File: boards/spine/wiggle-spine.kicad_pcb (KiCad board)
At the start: 2 copper layers, 114.3 x 88.9 mm, 187 parts, among them CON1 USB-B, CON2 XLR-3 Female, CON3 USB-A, CON4 2.5mm 5-24V 5A, CON5 5-24V 16A, CON6 PLR135, CON7 PLT133, Q1 DMN3190LDW, Q2 2N7002P, Q3 AOD4189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

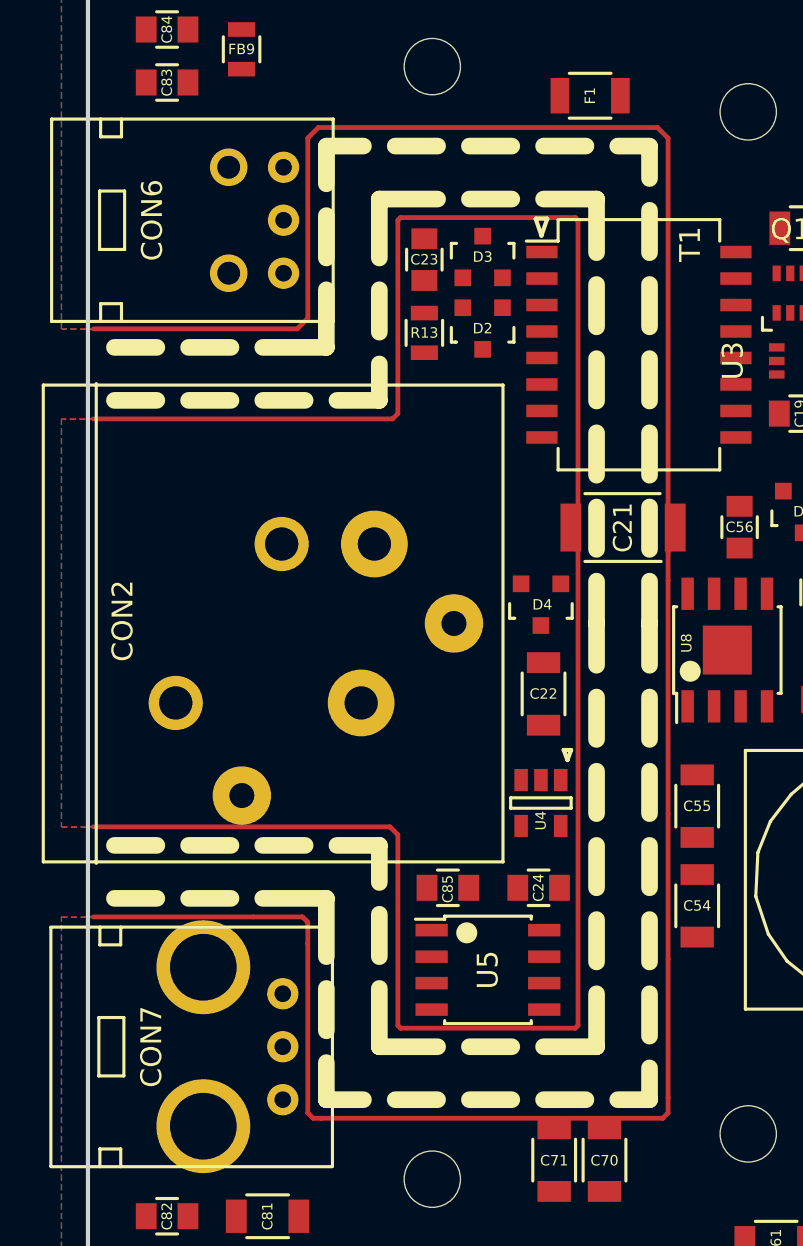
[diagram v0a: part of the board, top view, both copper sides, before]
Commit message: Hand edit to duplicate gap boundaries on bottom layer
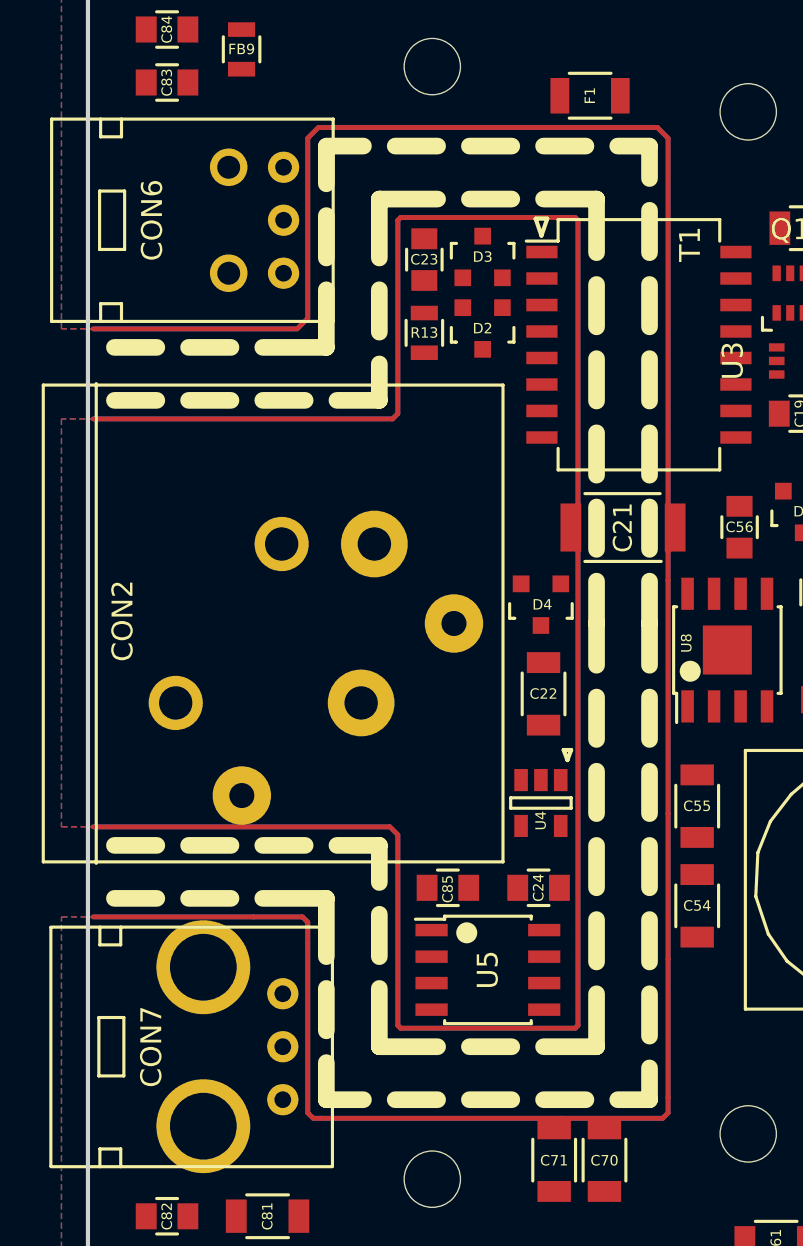
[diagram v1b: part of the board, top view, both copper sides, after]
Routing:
- net GND: track 120.9 -> 241.7 mm
- net /DMX512/DMXGND: track 104.3 -> 208.5 mm
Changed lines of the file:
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@@
   (segment (start 108.585 105.664) (end 108.585 82.129) (width 0.2286) (layer F.Cu) (net 172))
   (segment (start 108.585 82.129) (end 108.244 81.788) (width 0.2286) (layer F.Cu) (net 172))
+  (segment (start 112.649 110.109) (end 107.823 110.109) (width 0.2286) (layer B.Cu) (net 136))
+  (segment (start 93.035 100.457) (end 85.344 100.457) (width 0.2286) (layer B.Cu) (net 136))
+  (segment (start 95.377 100.457) (end 93.035 100.457) (width 0.2286) (layer B.Cu) (net 136))
+  (segment (start 95.540001 100.620001) (end 95.377 100.457) (width 0.2286) (layer B.Cu) (net 136))
+  (segment (start 95.631 100.711) (end 95.540001 100.620001) (width 0.2286) (layer B.Cu) (net 136))
+  (segment (start 95.631 101.727) (end 95.631 100.711) (width 0.2286) (layer B.Cu) (net 136))
+  (segment (start 95.631 109.855) (end 95.631 101.727) (width 0.2286) (layer B.Cu) (net 136))
+  (segment (start 95.885 110.109) (end 95.631 109.855) (width 0.2286) (layer B.Cu) (net 136))
+  (segment (start 96.266 110.109) (end 95.885 110.109) (width 0.2286) (layer B.Cu) (net 136))
+  (segment (start 107.823 110.109) (end 96.266 110.109) (width 0.2286) (layer B.Cu) (net 136))
+  (segment (start 112.903 109.855) (end 112.649 110.109) (width 0.2286) (layer B.Cu) (net 136))
+  (segment (start 112.903 109.118392) (end 112.903 109.855) (width 0.2286) (layer B.Cu) (net 136))
+  (segment (start 112.903 102.489) (end 112.903 109.118392) (width 0.2286) (layer B.Cu) (net 136))
+  (segment (start 112.903 95.504) (end 112.903 102.489) (width 0.2286) (layer B.Cu) (net 136))
+  (segment (start 112.903 84.328) (end 112.903 95.504) (width 0.2286) (layer B.Cu) (net 136))
+  (segment (start 112.903 84.328) (end 112.903 82.931) (width 0.2286) (layer B.Cu) (net 136))
+  (segment (start 113.244 82.59) (end 113.244 81.788) (width 0.2286) (layer B.Cu) (net 136))
+  (segment (start 112.903 82.931) (end 113.244 82.59) (width 0.2286) (layer B.Cu) (net 136))
+  (segment (start 85.344 72.263) (end 95.123 72.263) (width 0.2286) (layer B.Cu) (net 136))
+  (segment (start 112.395 62.611) (end 112.903 63.119) (width 0.2286) (layer B.Cu) (net 136))
+  (segment (start 112.903 81.447) (end 113.244 81.788) (width 0.2286) (layer B.Cu) (net 136))
+  (segment (start 95.123 72.263) (end 95.631 71.755) (width 0.2286) (layer B.Cu) (net 136))
+  (segment (start 95.631 71.755) (end 95.631 63.119) (width 0.2286) (layer B.Cu) (net 136))
+  (segment (start 95.631 63.119) (end 96.139 62.611) (width 0.2286) (layer B.Cu) (net 136))
+  (segment (start 96.139 62.611) (end 112.395 62.611) (width 0.2286) (layer B.Cu) (net 136))
+  (segment (start 112.903 63.119) (end 112.903 81.447) (width 0.2286) (layer B.Cu) (net 136))
+  (segment (start 85.344 76.581) (end 99.695 76.581) (width 0.2286) (layer B.Cu) (net 172))
+  (segment (start 99.949 67.056) (end 100.076 66.929) (width 0.2286) (layer B.Cu) (net 172))
+  (segment (start 108.585 81.447) (end 108.244 81.788) (width 0.2286) (layer B.Cu) (net 172))
+  (segment (start 99.695 76.581) (end 99.949 76.327) (width 0.2286) (layer B.Cu) (net 172))
+  (segment (start 99.949 76.327) (end 99.949 67.056) (width 0.2286) (layer B.Cu) (net 172))
+  (segment (start 100.076 66.929) (end 108.458 66.929) (width 0.2286) (layer B.Cu) (net 172))
+  (segment (start 108.458 66.929) (end 108.585 67.056) (width 0.2286) (layer B.Cu) (net 172))
+  (segment (start 108.585 67.056) (end 108.585 81.447) (width 0.2286) (layer B.Cu) (net 172))
+  (segment (start 85.344 96.139) (end 99.568 96.139) (width 0.2286) (layer B.Cu) (net 172))
+  (segment (start 99.568 96.139) (end 99.949 96.52) (width 0.2286) (layer B.Cu) (net 172))
+  (segment (start 99.949 96.52) (end 99.949 105.664) (width 0.2286) (layer B.Cu) (net 172))
+  (segment (start 99.949 105.664) (end 100.076 105.791) (width 0.2286) (layer B.Cu) (net 172))
+  (segment (start 100.076 105.791) (end 108.458 105.791) (width 0.2286) (layer B.Cu) (net 172))
+  (segment (start 108.458 105.791) (end 108.585 105.664) (width 0.2286) (layer B.Cu) (net 172))
+  (segment (start 108.585 105.664) (end 108.585 82.129) (width 0.2286) (layer B.Cu) (net 172))
+  (segment (start 108.585 82.129) (end 108.244 81.788) (width 0.2286) (layer B.Cu) (net 172))
   (zone (net 136) (net_name GND) (layer F.Cu) (hatch edge 0.508)
     (connect_pads yes (clearance 0.381))

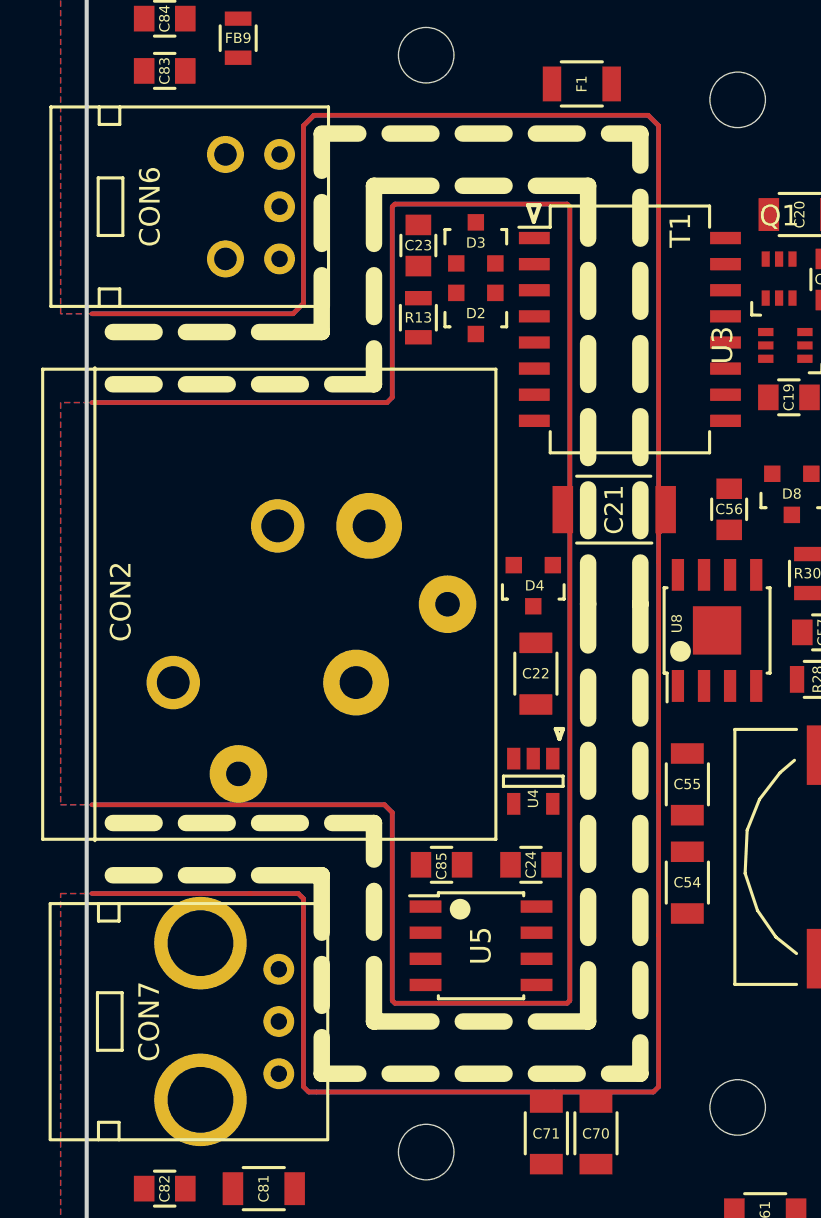
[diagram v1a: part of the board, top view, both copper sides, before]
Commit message: Via stitching and net fixes for DMXGND
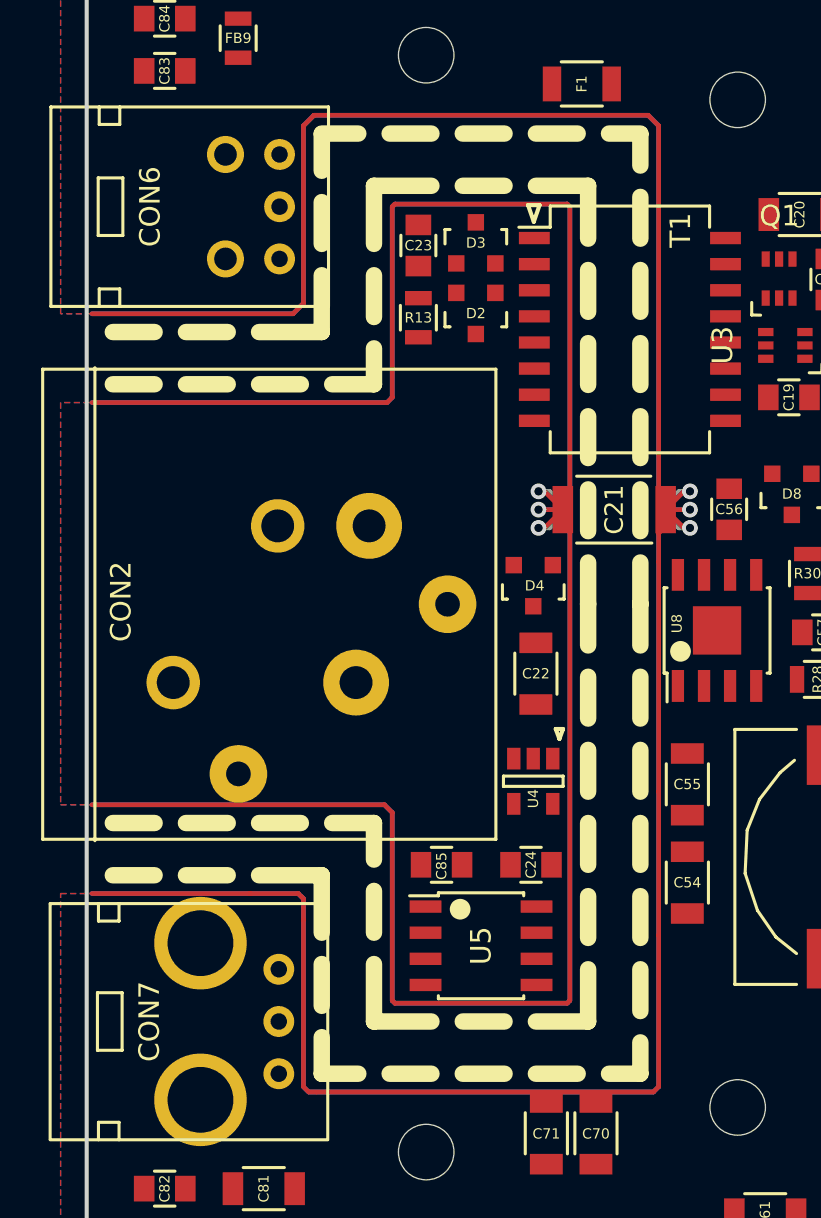
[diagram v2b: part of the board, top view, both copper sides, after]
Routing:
- net GND: track 241.7 -> 250.9 mm, vias 0 -> 3
- net /DMX512/DMXGND: track 208.5 -> 217.7 mm, vias 0 -> 3

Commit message: More zone placement.. concerned about +24
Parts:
- moved R20 46.5 mm to (156.0, 77.0), turned to 180 degrees
- moved C73 16.9 mm to (183.6, 69.6), turned to 0 degrees
- moved R35 11.8 mm to (181.3, 67.3), turned to 0 degrees
- moved D9 11.7 mm to (177.5, 67.8), turned to 0 degrees
- moved FB3 9.80 mm to (172.0, 81.8), turned to 0 degrees
- moved C72 2.92 mm to (188.7, 65.3)
- moved R17 2.79 mm to (197.4, 54.2)
- moved R19 2.79 mm to (193.3, 54.2)
- moved R18 2.79 mm to (195.3, 54.2)
- moved C1 1.42 mm to (165.9, 79.0)
- moved C43 0.64 mm to (170.7, 74.5)
- moved C44 0.51 mm to (178.1, 74.5)
- moved Q3 0.25 mm to (183.6, 56.4)
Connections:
- net Net-(C72-Pad2) renamed /Power/5-24V Power Input/POWER_IN
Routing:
- net +24V: track 0.00 -> 245.4 mm
- net GNDPWR: track 0.00 -> 62.8 mm
- net /Power/5-24V Power Input/POWER_IN: track 0.00 -> 25.8 mm
- net GND: track 250.9 -> 268.7 mm
- net +5V: track 0.00 -> 17.8 mm
- net +3V3: track 0.00 -> 17.8 mm
- net Net-(D9-Pad3): track 0.00 -> 13.3 mm
- added copper zone on F.Cu, net +24V
- added copper zone on F.Cu, net /Power/5-24V Power Input/POWER_IN
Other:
- net class ExtPower removed
- net class ProtectiveGround removed

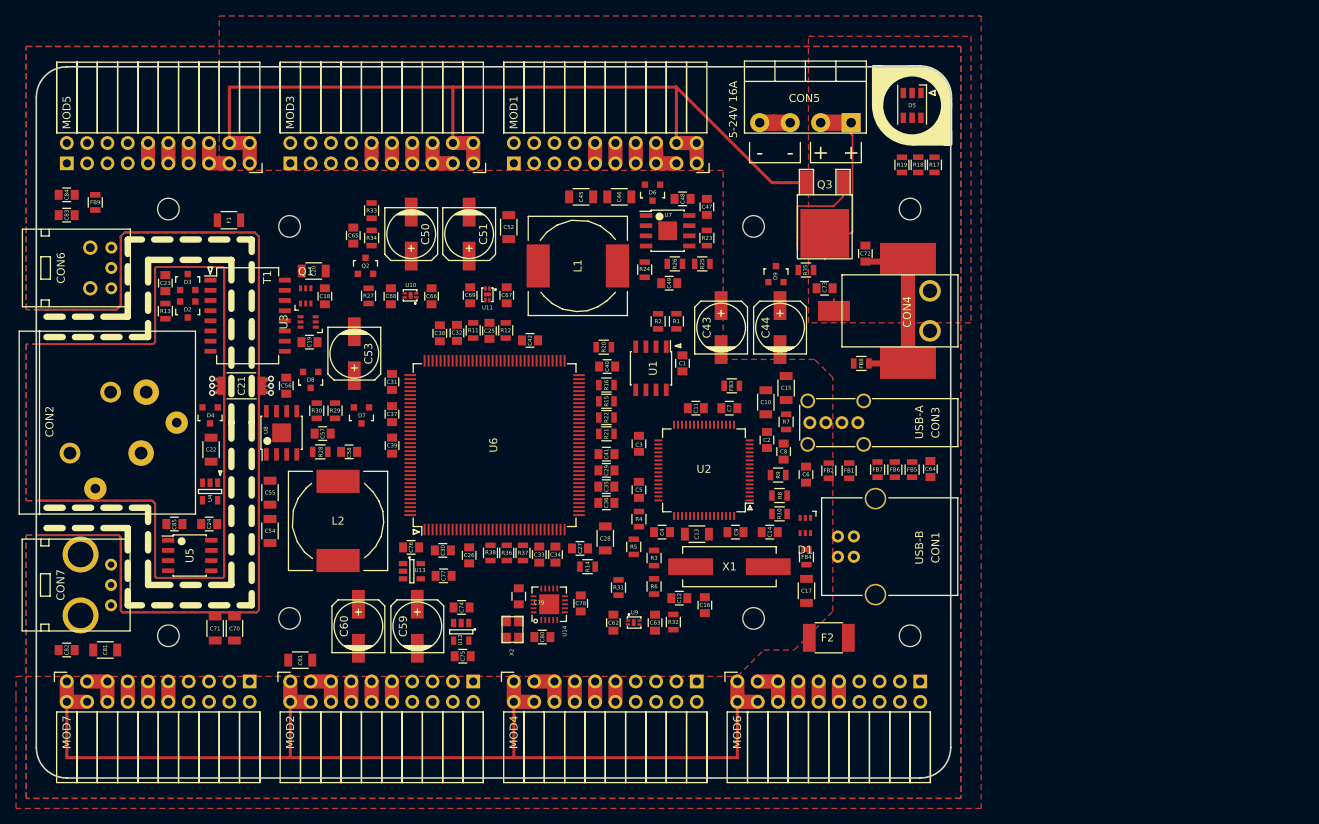
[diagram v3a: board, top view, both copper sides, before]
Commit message: Progress on zone and 3v3 filter layout
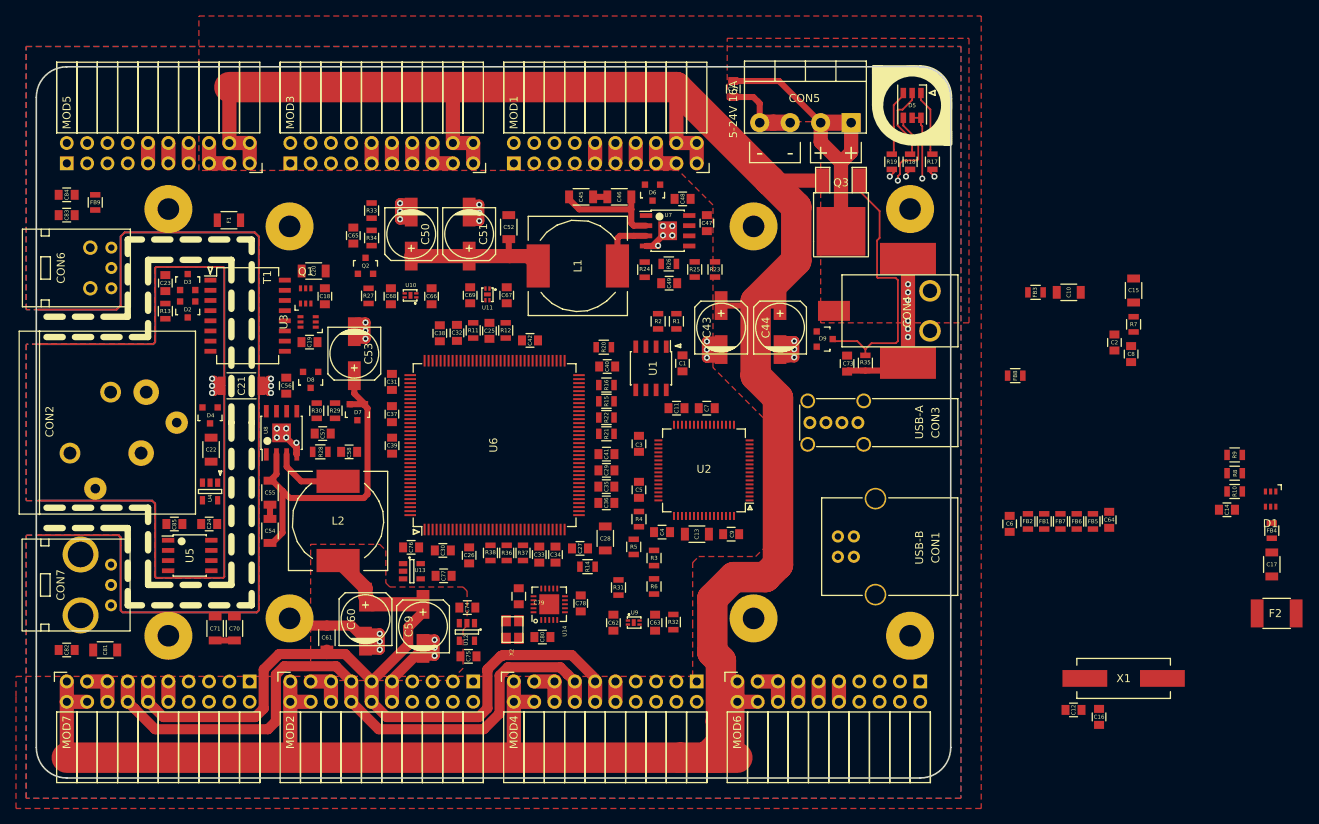
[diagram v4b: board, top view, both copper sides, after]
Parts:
- moved C17 58.3 mm to (239.5, 104.1)
- moved D1 58.3 mm to (239.4, 95.9)
- moved FB4 58.3 mm to (239.5, 99.9)
- moved C14 57.2 mm to (233.9, 97.3)
- moved R9 57.1 mm to (234.9, 90.4)
- moved R10 57.0 mm to (234.9, 95.0)
- moved R8 57.0 mm to (234.9, 92.7)
- moved F2 56.1 mm to (240.1, 110.2)
- moved C12 51.2 mm to (214.7, 122.3)
- moved X1 51.2 mm to (221.0, 118.4)
- moved C16 51.2 mm to (217.9, 123.2)
- moved C8 45.1 mm to (221.9, 77.8)
- moved C15 45.1 mm to (222.2, 69.9)
- moved C2 45.1 mm to (219.9, 76.4)
- moved R7 45.1 mm to (222.2, 74.1)
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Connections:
- REF** pad 1: (no net) -> GND (x5)
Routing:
- net +5V: track 17.8 -> 143.5 mm, vias 0 -> 1
- net +24V: track 245.4 -> 358.6 mm
- net +3V3: track 17.8 -> 127.0 mm, vias 0 -> 1
- net GND: track 268.7 -> 348.3 mm, vias 3 -> 34
- net Net-(D9-Pad3): track 13.3 -> 33.5 mm
- net /Power/USB Power Output/5V_IN: track 0.00 -> 18.6 mm
- net /Power/5-24V Power Input/POWER_IN: track 25.8 -> 37.3 mm
- net Net-(D5-Pad2): track 0.00 -> 9.47 mm
- net Net-(C57-Pad1): track 0.00 -> 8.72 mm
- net Net-(D5-Pad3): track 0.00 -> 8.15 mm
- net Net-(D5-Pad1): track 0.00 -> 8.14 mm
- net Net-(C48-Pad1): track 0.00 -> 7.16 mm
- net GNDPWR: track 62.8 -> 67.1 mm, vias 0 -> 6
- net /FPGA/GREEN_N: track 0.00 -> 1.28 mm, vias 0 -> 1
- net /FPGA/BLUE_N: track 0.00 -> 1.10 mm, vias 0 -> 1
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- added copper zone on F.Cu, net +3V3
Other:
- rule pad_to_mask_clearance: 0.2 -> 0.254
